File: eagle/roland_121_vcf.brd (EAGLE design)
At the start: 99.4 x 67.9 mm, 100 parts, among them IC1 TL072P, IC2 LM13700N, IC3 LM13700N, Q1 2SK30, Q2 2N3904, Q3 2N3906, Q4 2SK30, Q5 2N3904, Q6 2SK30, Q8 2N3904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

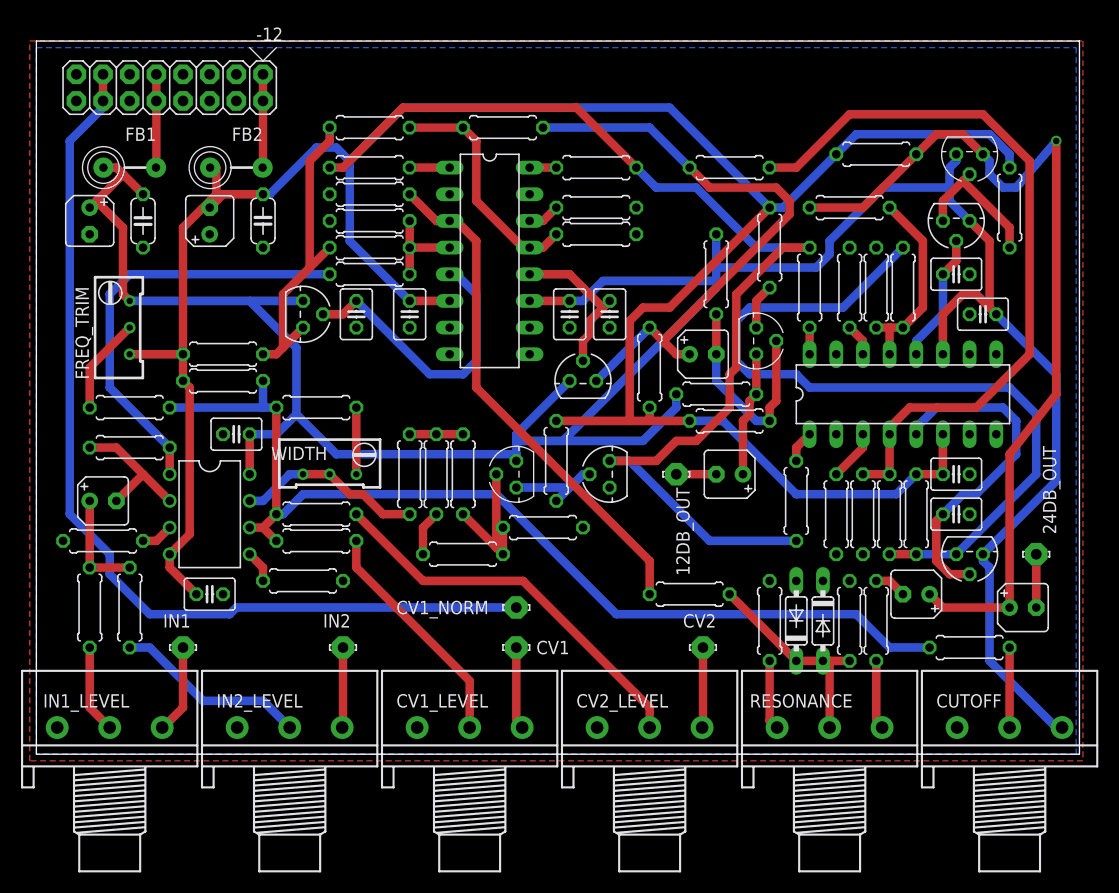
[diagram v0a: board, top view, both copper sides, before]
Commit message: smt decouplers, shrouded power, 16 or 9mm pots
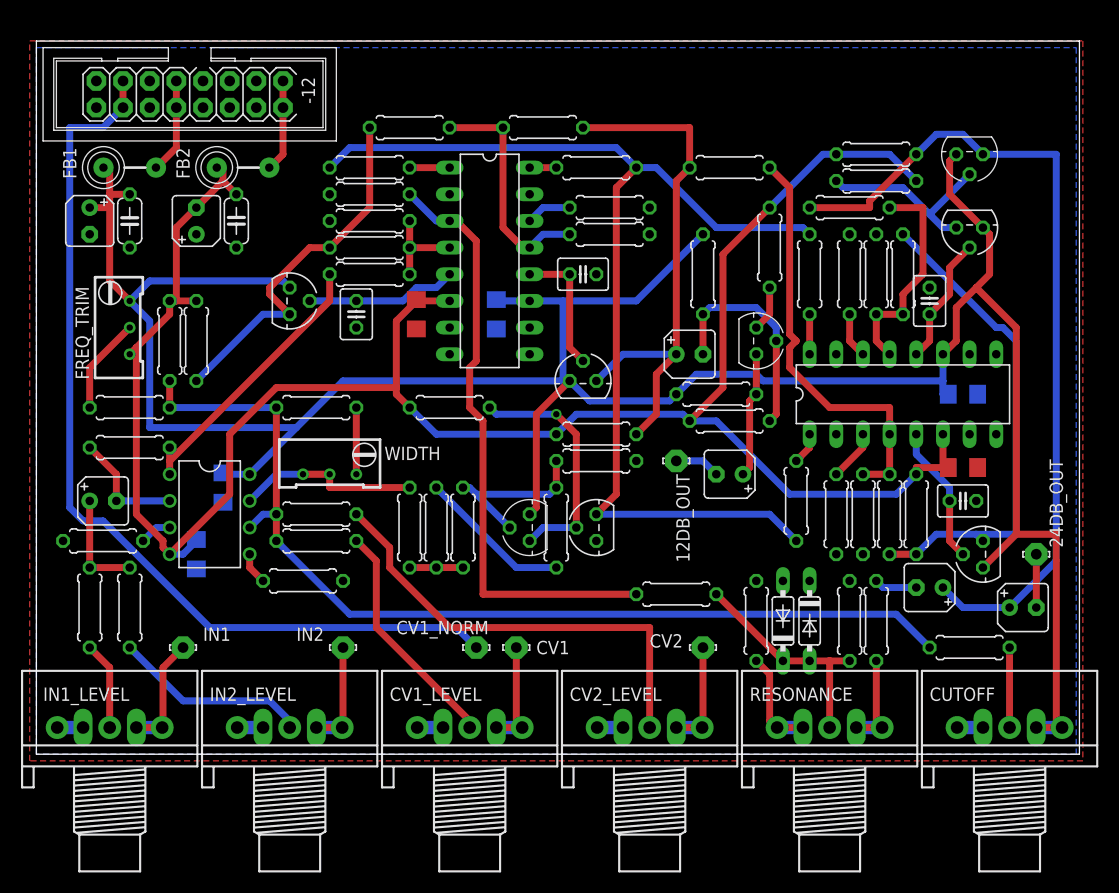
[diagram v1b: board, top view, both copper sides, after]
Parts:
- C3, C4, C5, C6, C7, C8: value 0.1uF -> 100n; device rcl:C025-030X050 -> rcl:C1206
- moved R57 13.0 mm to (80.0, 54.6), turned to 180 degrees
- moved R30 11.4 mm to (39.4, 33.0), turned to 180 degrees
- moved R25 9.25 mm to (49.5, 21.6), turned to 270 degrees
- moved R28 8.13 mm to (53.3, 27.9)
- moved R38 8.13 mm to (53.3, 30.5), turned to 0 degrees
- moved C7 7.85 mm to (88.3, 34.3), flipped to the bottom
- moved C5 6.98 mm to (43.8, 41.9), flipped to the bottom
- moved R13 6.35 mm to (12.7, 39.4), turned to 90 degrees
- moved CV1_NORM 5.39 mm to (41.9, 10.2)
- moved C3 5.24 mm to (17.8, 25.4), flipped to the bottom, turned to 270 degrees
- moved Q2 5.24 mm to (47.0, 21.6)
- moved Q3 5.24 mm to (53.3, 21.6)
- moved R21 5.08 mm to (35.6, 21.6), turned to 90 degrees
- moved R23 5.08 mm to (38.1, 21.6), turned to 270 degrees
- moved R24 5.08 mm to (40.6, 21.6), turned to 270 degrees
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- renumbered C19 to C2
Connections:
- net +12V: now also CUTOFF.6
- net GND: now also CUTOFF.4, CV1_LEVEL.4, CV2_LEVEL.4, IN1_LEVEL.4, IN2_LEVEL.4
- net N$34: now also IN2_LEVEL.6
- net N$48: now also RESONANCE.4
- net N$51: now also RESONANCE.6
- net N$54: now also CV2_LEVEL.6
- net N$58: now also IN1_LEVEL.6
- net N$59: now also CV1_LEVEL.6
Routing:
- net -12V: track 232.9 -> 198.1 mm
- net N$15: track 70.3 -> 40.4 mm
- net N$37: track 76.1 -> 47.2 mm
- net N$42: track 32.4 -> 13.3 mm
- net N$8: track 41.3 -> 26.6 mm
- net N$21: track 9.31 -> 23.2 mm, vias 0 -> 1
- net N$40: track 28.2 -> 14.4 mm
- net N$18: track 4.34 -> 14.6 mm
- net N$23: track 48.7 -> 57.2 mm
- net +12V: track 253.8 -> 261.1 mm
- net N$35: track 56.8 -> 50.1 mm
- net N$36: track 85.4 -> 79.7 mm, vias 1 -> 0
- net N$10: track 37.5 -> 43.1 mm
- net N$47: track 13.7 -> 18.7 mm
- net N$28: track 30.4 -> 35.2 mm
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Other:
- board text added: "Thanks to LFlab!"

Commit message: now with flexible trimmer pinout
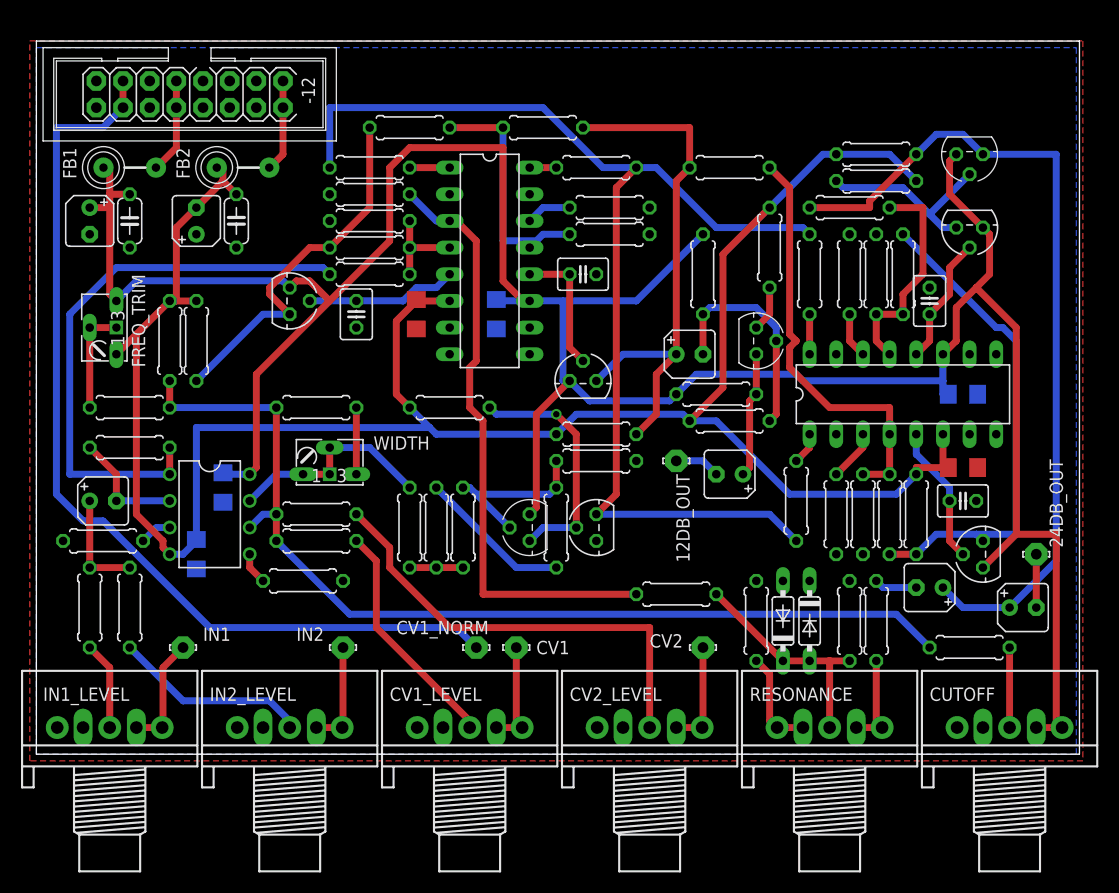
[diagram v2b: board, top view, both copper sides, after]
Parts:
- FREQ_TRIM, WIDTH: device rcl:RTRIM64W -> pot:B64W
- moved WIDTH 1.27 mm to (27.9, 26.7), turned to 180 degrees
- turned FREQ_TRIM to 270 degrees
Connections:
- removed net N$13: IC1.7, R21.2, WIDTH.1, WIDTH.2
- new net N$38: IC1.7, R21.2, WIDTH.A, WIDTH.P$1, WIDTH.S
- net +12V: now also FREQ_TRIM.E; no longer FREQ_TRIM.3
- net -12V: now also FREQ_TRIM.A; no longer FREQ_TRIM.1
- net N$17: now also FREQ_TRIM.P$1, FREQ_TRIM.S; no longer FREQ_TRIM.2
- net N$9: now also WIDTH.E; no longer WIDTH.3
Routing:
- net N$8: track 26.6 -> 54.2 mm
- net N$38: track 0.00 -> 20.4 mm
- net N$13: track 17.6 -> 0.00 mm
- net +12V: track 261.1 -> 268.7 mm
- net N$45: track 104.6 -> 111.1 mm
- net -12V: track 198.1 -> 201.3 mm
- net N$55: track 88.9 -> 90.7 mm
- net N$3: track 22.3 -> 23.4 mm
- net N$17: track 9.20 -> 10.2 mm
